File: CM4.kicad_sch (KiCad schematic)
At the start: 11 parts, among them J11 Conn_02x05_Odd_Even, J6 HDMI_A_2.0, U1 RaspberryPi-CM4Lite, U100 DF40C-100DS-0.4V(51), U101 DF40C-100DS-0.4V(51)

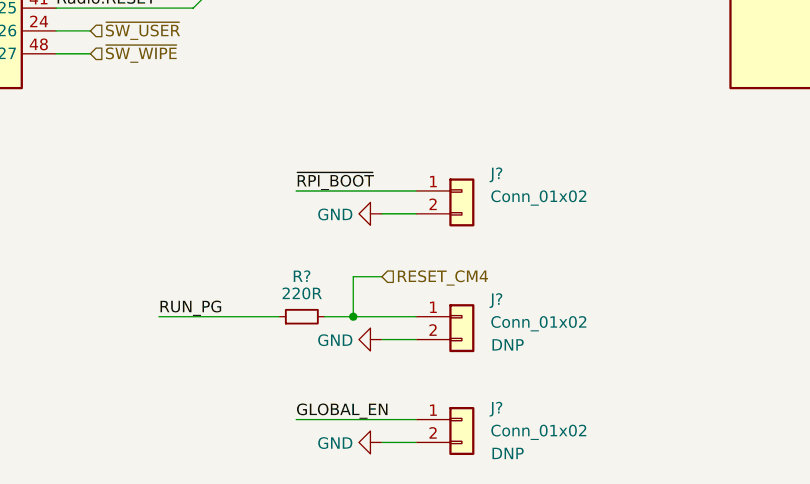
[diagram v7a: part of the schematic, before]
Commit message: Assign footprints and annotate components
Signed-off-by: Stefan Agner <stefan@agner.ch>
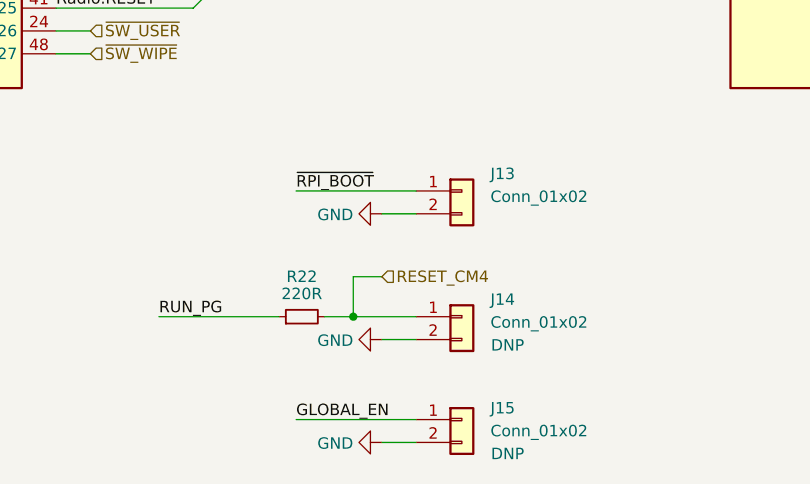
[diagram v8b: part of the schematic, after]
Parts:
- J13, J14, J15: renamed from J?; footprint (none) -> Connector_PinHeader_2.54mm:PinHeader_1x02_P2.54mm_Vertical
- R22: renamed from R?; footprint (none) -> Resistor_SMD:R_0402_1005Metric
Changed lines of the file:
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@@
     (comment 2 "Light Blue")
   )
+  (bus_alias "UART" (members "TXD" "RXD" "CTS" "RTS"))
+  (bus_alias "HDMI" (members "D0+" "D0-" "D1+" "D1-" "D2+" "D2-" "CLK+" "CLK-" "CEC" "HPD" "SDA" "SCL"))
+  (bus_alias "SD" (members "D[0..3]" "CMD" "CLK" "PWR" "DET"))
   (bus_alias "PCIe" (members "~RST" "~CLKREQ" "CLK+" "CLK-" "TX+" "TX-" "RX+" "RX-"))
-  (bus_alias "SD" (members "D[0..3]" "CMD" "CLK" "PWR" "DET"))
-  (bus_alias "HDMI" (members "D0+" "D0-" "D1+" "D1-" "D2+" "D2-" "CLK+" "CLK-" "CEC" "HPD" "SDA" "SCL"))
-  (bus_alias "UART" (members "TXD" "RXD" "CTS" "RTS"))
   (junction (at 59.055 173.99) (diameter 0.9144) (color 0 0 0 0))
   (junction (at 121.92 171.45) (diameter 0.9144) (color 0 0 0 0))
@@
   (symbol (lib_id "Device:R_Small") (at 116.205 171.45 90) (unit 1)
     (in_bom yes) (on_board yes)
-    (property "Reference" "R?" (id 0) (at 116.205 167.005 90))
+    (property "Reference" "R22" (id 0) (at 116.205 167.005 90))
     (property "Value" "220R" (id 1) (at 116.205 168.91 90))
-    (property "Footprint" "" (id 2) (at 116.205 171.45 0)
+    (property "Footprint" "Resistor_SMD:R_0402_1005Metric" (id 2) (at 116.205 171.45 0)
       (effects (font (size 1.27 1.27)) hide)
     )
@@
   (symbol (lib_id "Connector_Generic:Conn_01x02") (at 133.985 157.48 0) (unit 1)
     (in_bom yes) (on_board yes)
-    (property "Reference" "J?" (id 0) (at 137.16 155.5749 0)
+    (property "Reference" "J13" (id 0) (at 137.16 155.5749 0)
       (effects (font (size 1.27 1.27)) (justify left))
     )
@@
       (effects (font (size 1.27 1.27)) (justify left))
     )
-    (property "Footprint" "" (id 2) (at 133.985 157.48 0)
+    (property "Footprint" "Connector_PinHeader_2.54mm:PinHeader_1x02_P2.54mm_Vertical" (id 2) (at 133.985 157.48 0)
       (effects (font (size 1.27 1.27)) hide)
     )
@@
   (symbol (lib_id "Connector_Generic:Conn_01x02") (at 133.985 171.45 0) (unit 1)
     (in_bom yes) (on_board yes)
-    (property "Reference" "J?" (id 0) (at 137.16 169.5449 0)
+    (property "Reference" "J14" (id 0) (at 137.16 169.5449 0)
       (effects (font (size 1.27 1.27)) (justify left))
     )
@@
       (effects (font (size 1.27 1.27)) (justify left))
     )
-    (property "Footprint" "" (id 2) (at 133.985 171.45 0)
+    (property "Footprint" "Connector_PinHeader_2.54mm:PinHeader_1x02_P2.54mm_Vertical" (id 2) (at 133.985 171.45 0)
       (effects (font (size 1.27 1.27)) hide)
     )
@@
   (symbol (lib_id "Connector_Generic:Conn_01x02") (at 133.985 182.88 0) (unit 1)
     (in_bom yes) (on_board yes)
-    (property "Reference" "J?" (id 0) (at 137.16 181.6099 0)
+    (property "Reference" "J15" (id 0) (at 137.16 181.6099 0)
       (effects (font (size 1.27 1.27)) (justify left))
     )
@@
       (effects (font (size 1.27 1.27)) (justify left))
     )
-    (property "Footprint" "" (id 2) (at 133.985 182.88 0)
-      (effects (font (size 1.27 1.27)) hide)
-    )
+    (property "Footprint" "Connector_PinHeader_2.54mm:PinHeader_1x02_P2.54mm_Vertical" (id 2) (at 133.985 182.88 0)
+      (effects (font (size 1.27 1.27)) hide)
+    )
